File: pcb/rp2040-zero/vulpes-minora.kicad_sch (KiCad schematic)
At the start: 58 parts, among them J13 Conn_01x04_Female, J2 AudioJack4dpb, J3 AudioJack4dpb, SW10 SW_Push, SW11 SW_Push, SW12 SW_Push, SW14 SW_Push, SW15 SW_Push, SW16 SW_Push, SW17 SW_Push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

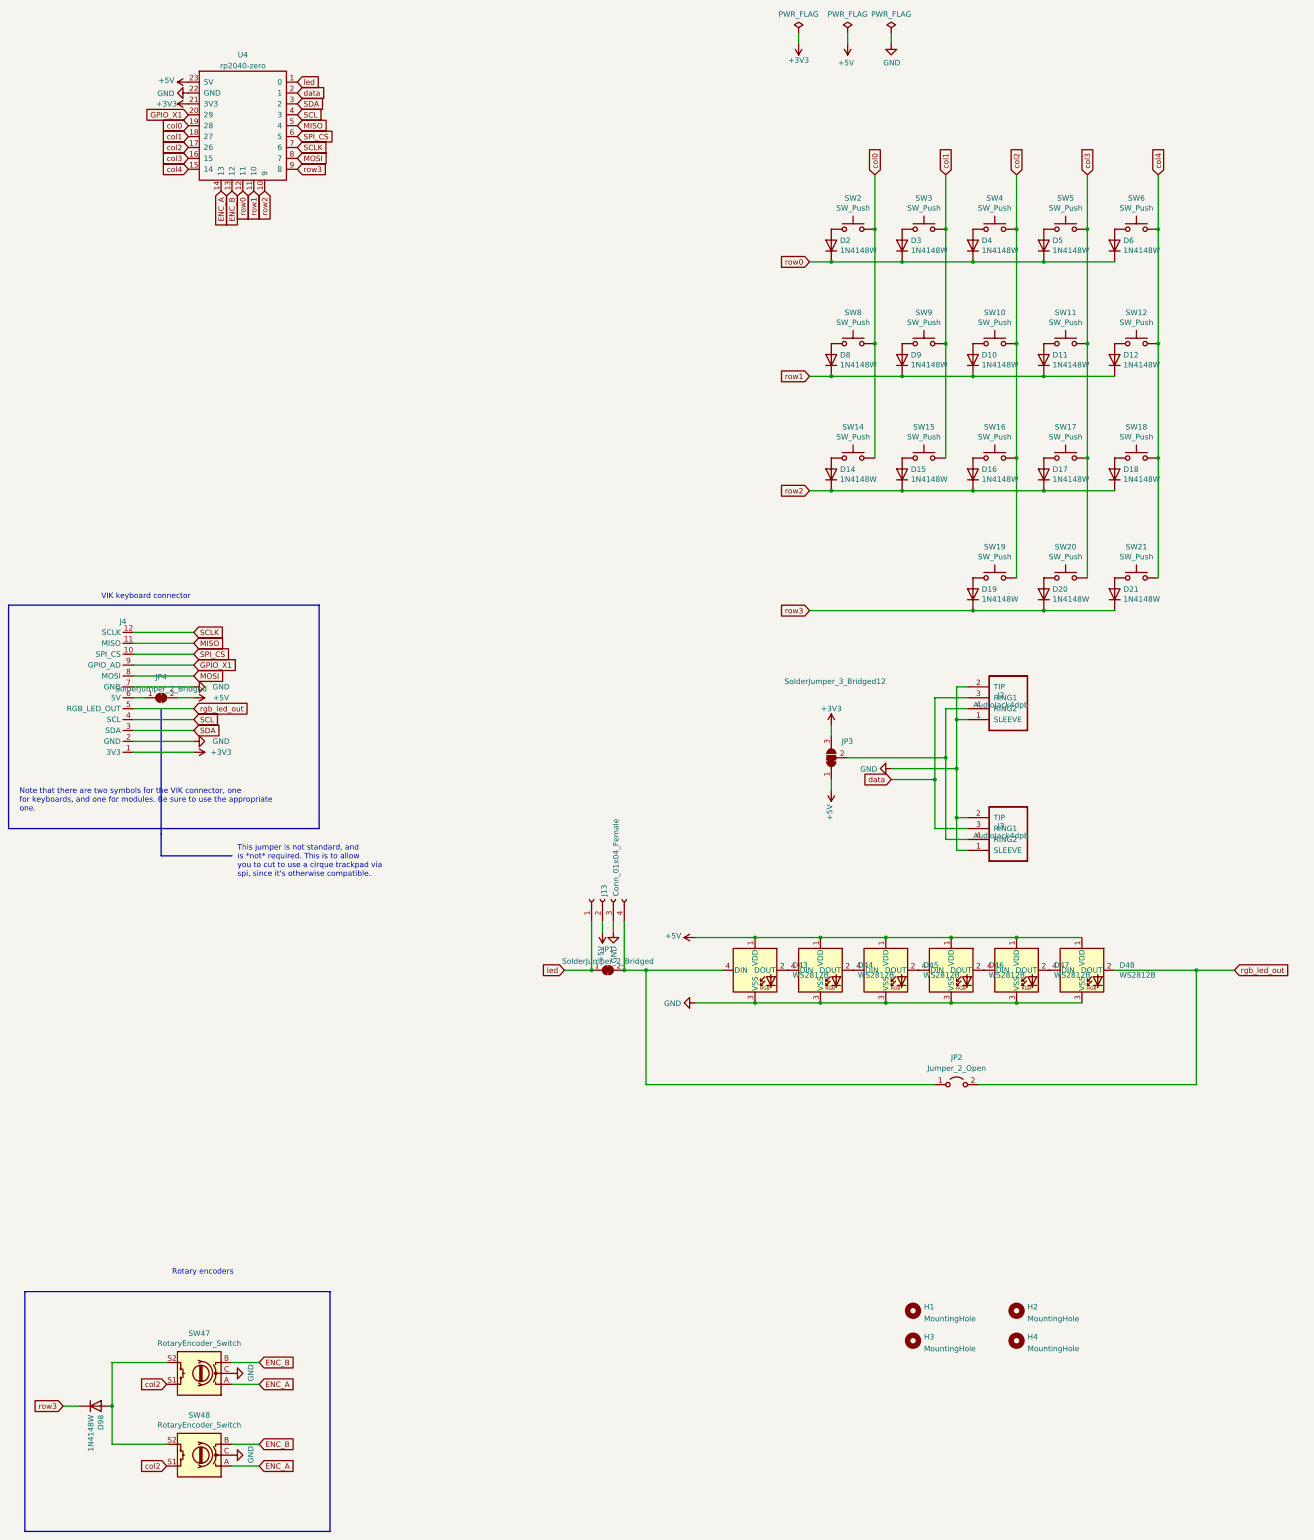
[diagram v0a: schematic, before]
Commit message: updated vulpes minora to match new vik standard of two gpio, corresponding to commit 57a4fb79db6f66c8cfaf2971141367c47d66a44f in the vik repo
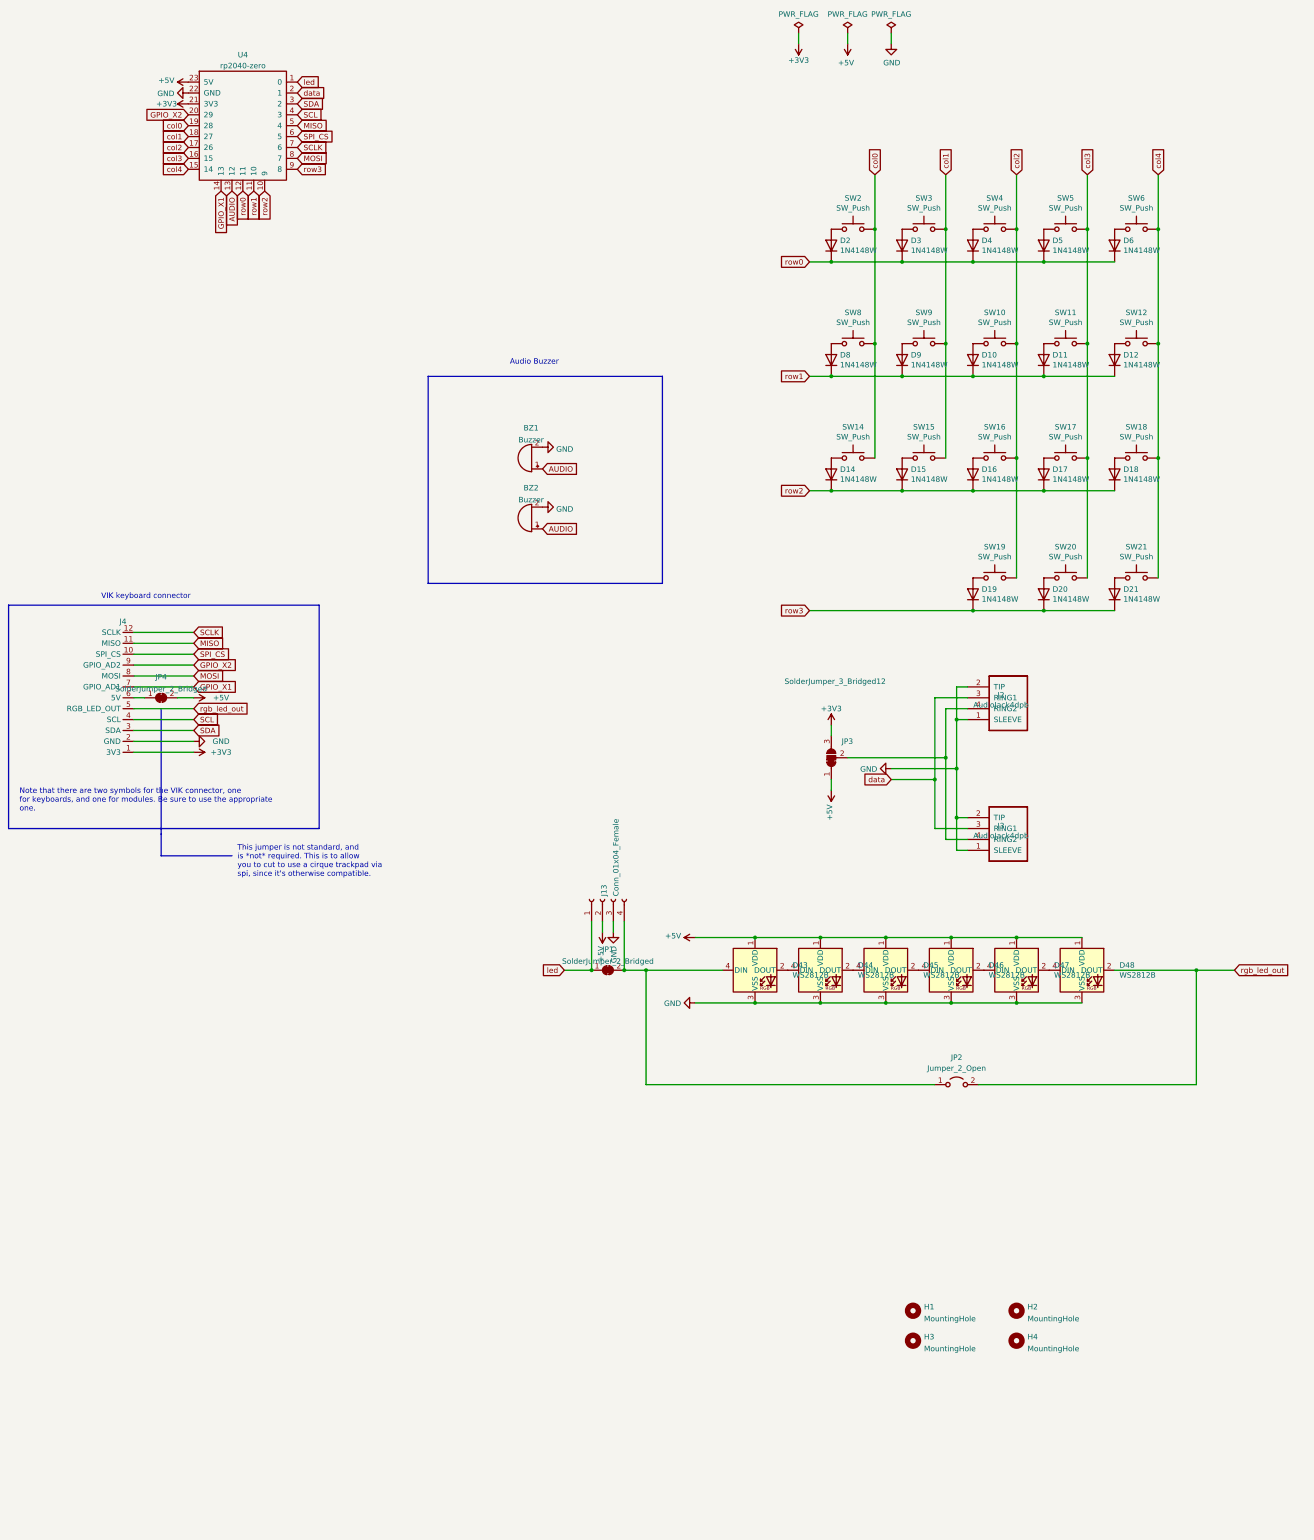
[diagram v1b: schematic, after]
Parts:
- removed D98: 1N4148W, Diode_SMD:D_SOD-123, symbol Diode:1N4148W
- removed SW47, SW48: RotaryEncoder_Switch, fingerpunch:RotaryEncoder_EC11-no-legs, symbol ffkb-rescue:RotaryEncoder_Switch-Device
- added BZ1, BZ2: Buzzer, fingerpunch:AST1109MLTRQ, symbol Device:Buzzer
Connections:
- net ENC_A is gone; now on net GPIO_X1: U4.14 (13)
- net GND: now also BZ1.2 (+), BZ2.2 (+); no longer J4.7 (GND)
- net GPIO_X1: now also J4.7 (GPIO_AD1); no longer J4.9 (GPIO_AD), U4.20 (29)
- net ENC_B renamed AUDIO
- net AUDIO: now also BZ1.1 (-), BZ2.1 (-)
- new net GPIO_X2: J4.9 (GPIO_AD2), U4.20 (29)
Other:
- note added: "Audio Buzzer"
- note removed: "Rotary encoders"
